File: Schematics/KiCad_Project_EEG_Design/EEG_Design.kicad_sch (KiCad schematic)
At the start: 2 parts, among them U1 INA819ID

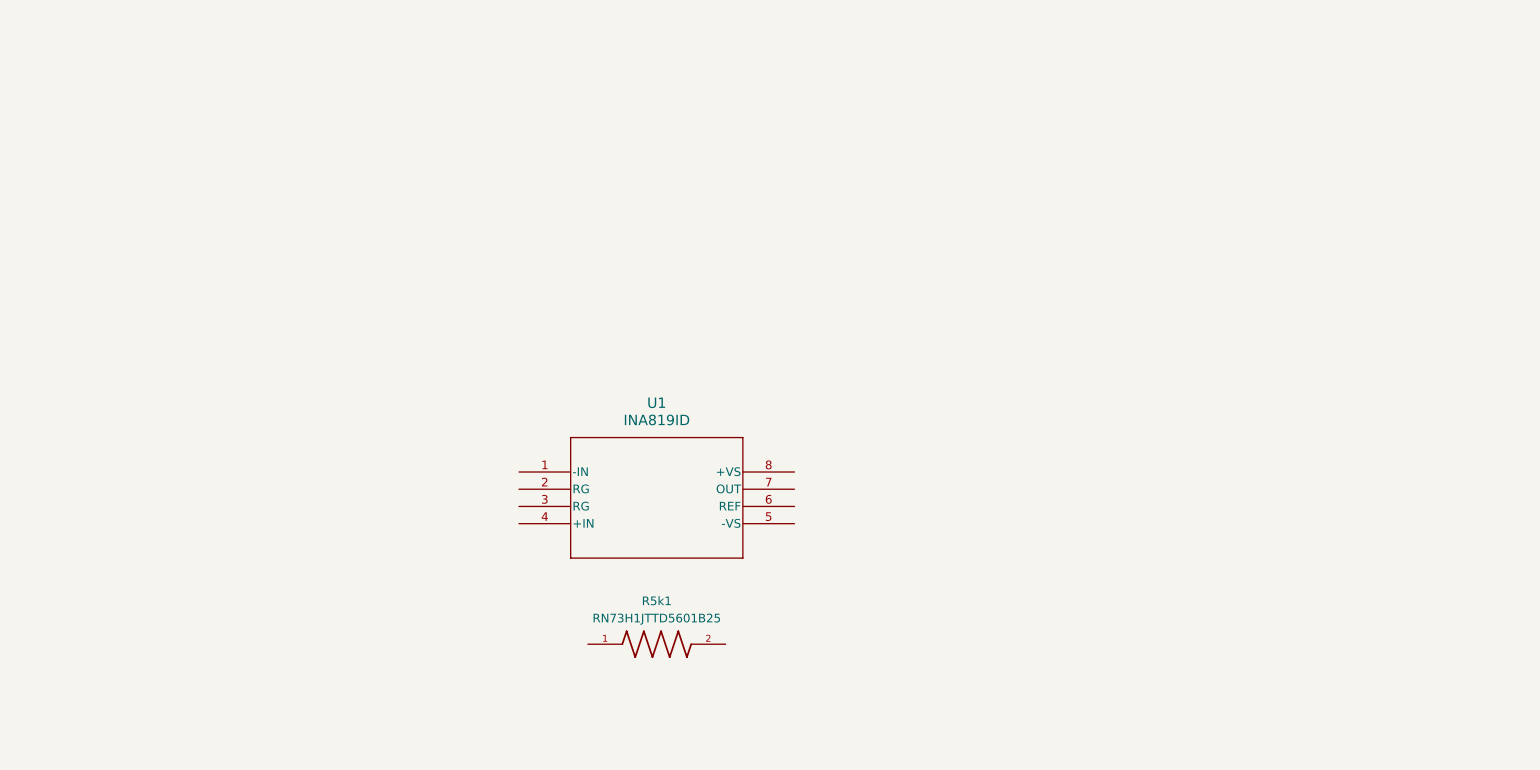
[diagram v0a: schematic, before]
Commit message: Updated spreadsheet & schematic
Added the following/
- Added chosen diode and op amp for components spreadsheet
- Created schematic file in KiCad
- Updated KiCad component library with added diode and op amp
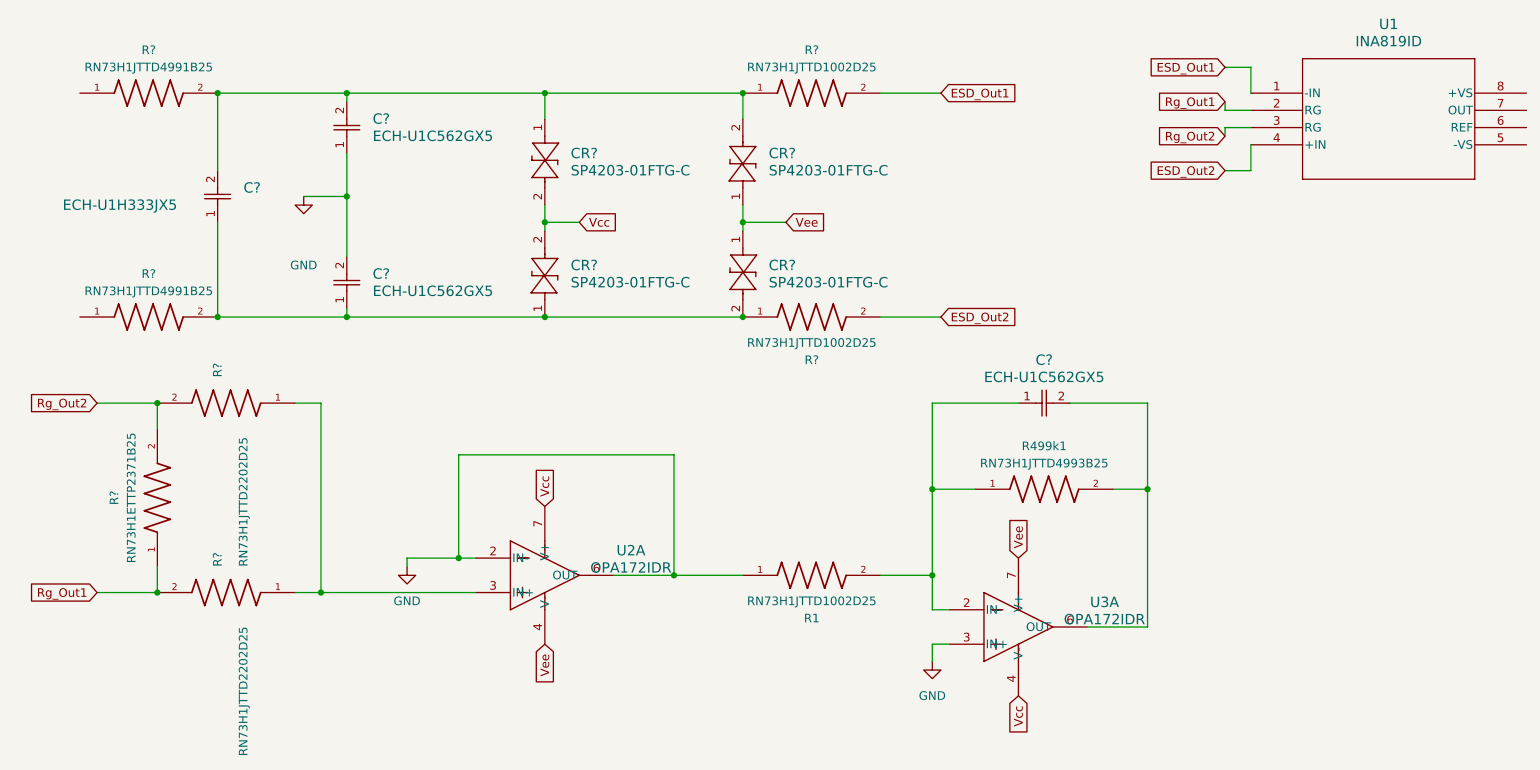
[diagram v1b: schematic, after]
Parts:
- removed R5k1: RN73H1JTTD5601B25, RN73H1JTTD5601B25:RESC1608X55N, symbol EEG part lib:RN73H1JTTD5601B25
- added C? (x3): ECH-U1C562GX5, CAP_J1_PAN, symbol EEG part lib:ECH-U1C562GX5
- added C?: ECH-U1H333JX5, CAP_G3_PAN, symbol EEG part lib:ECH-U1H333JX5
- added CR? (x4): SP4203-01FTG-C, ZDO_SP4203_LTF, symbol EEG part lib:SP4203-01FTG-C
- added R1, R? (x2): RN73H1JTTD1002D25, RN73H1JTTD1002D25:RESC1608X55N, symbol EEG part lib:RN73H1JTTD1002D25
- added R499k1: RN73H1JTTD4993B25, RN73H1JTTD4993B25:RESC1608X55N, symbol EEG part lib:RN73H1JTTD4993B25
- added R?: RN73H1ETTP2371B25, RN73H1ETTP2371B25:RESC1005X40N, symbol EEG part lib:RN73H1ETTP2371B25
- added R? (x2): RN73H1JTTD4991B25, RN73H1JTTD4991B25:RESC1608X55N, symbol EEG part lib:RN73H1JTTD4991B25
- added R? (x2): RN73H1JTTD2202D25, RN73H1JTTD2202D25:RESC1608X55N, symbol EEG part lib:RN73H1JTTD2202D25
- added U2, U3: OPA172IDR, D0008A_N, symbol EEG part lib:OPA172IDR
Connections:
- net ESD_Out1: now reaches U1.1 (-IN)
- net ESD_Out1: now also R?.2
- net Rg_Out1: now reaches U1.2 (RG)
- net Rg_Out1: now also R?.1, R?.2
- net Rg_Out2: now reaches U1.3 (RG)
- net Rg_Out2: now also R?.2, R?.2
- net ESD_Out2: now reaches U1.4 (+IN)
- net ESD_Out2: now also R?.2
- new net: C?.1, R1.2, R499k1.1, U3.2 (IN-)
- new net: C?.2, R499k1.2, U3.6 (OUT)
- new net: C?.2, C?.2, CR?.1, CR?.2, R?.1, R?.2
- new net: R?.1, R?.1, U2.3 (IN+)
- new net: C?.1, C?.1, CR?.1, CR?.2, R?.1, R?.2
- new net GND: C?.1, C?.2, R1.1, U2.2 (IN-), U2.6 (OUT), U3.3 (IN+)
- new net Vcc: CR?.2, CR?.2, U2.7 (V+), U3.4 (V-)
- new net Vee: CR?.1, CR?.1, U2.4 (V-), U3.7 (V+)
